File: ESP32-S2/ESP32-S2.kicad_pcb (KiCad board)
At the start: 2 copper layers, 27.9 x 70 mm, 39 parts, among them J1 Conn_01x18_Male, J2 Conn_01x21_Male, J3 USB_A, J4 TYPE-C-31-M-12, Q2 L8050QLT1G, Q3 L8050QLT1G, SW1 EN/RESET, SW2 BOOT/SELECT, U2 ESP32-S2-WROOM-ESP32-S2-WROOM, U3 AMS1117-3.3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

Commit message: Routing Updates
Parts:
- moved SW2 0.39 mm to (159.2, 119.5)
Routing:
- net GND: track 174.1 -> 108.1 mm, vias 8 -> 5
- net /GPIO0: track 82.5 -> 107.3 mm, vias 10 -> 6
- net /CHIP_PU: track 78.7 -> 83.2 mm
- net /GPIO19: track 50.1 -> 52.8 mm
- net /GPIO11: track 21.0 -> 18.4 mm
- net /GPIO12: track 22.4 -> 20.1 mm
- net /GPIO10: track 18.9 -> 16.9 mm
- net /TXD0: track 46.6 -> 44.8 mm
- net /DN1: track 43.2 -> 41.5 mm
- net /GPIO9: track 16.8 -> 15.3 mm
- net /GPIO15: track 22.6 -> 21.3 mm, vias 2 -> 0
- net /GPIO26: track 18.9 -> 18.4 mm
- net /GPIO17: track 33.9 -> 34.3 mm, vias 2 -> 0
- net /GPIO20: track 76.3 -> 76.6 mm, vias 4 -> 2

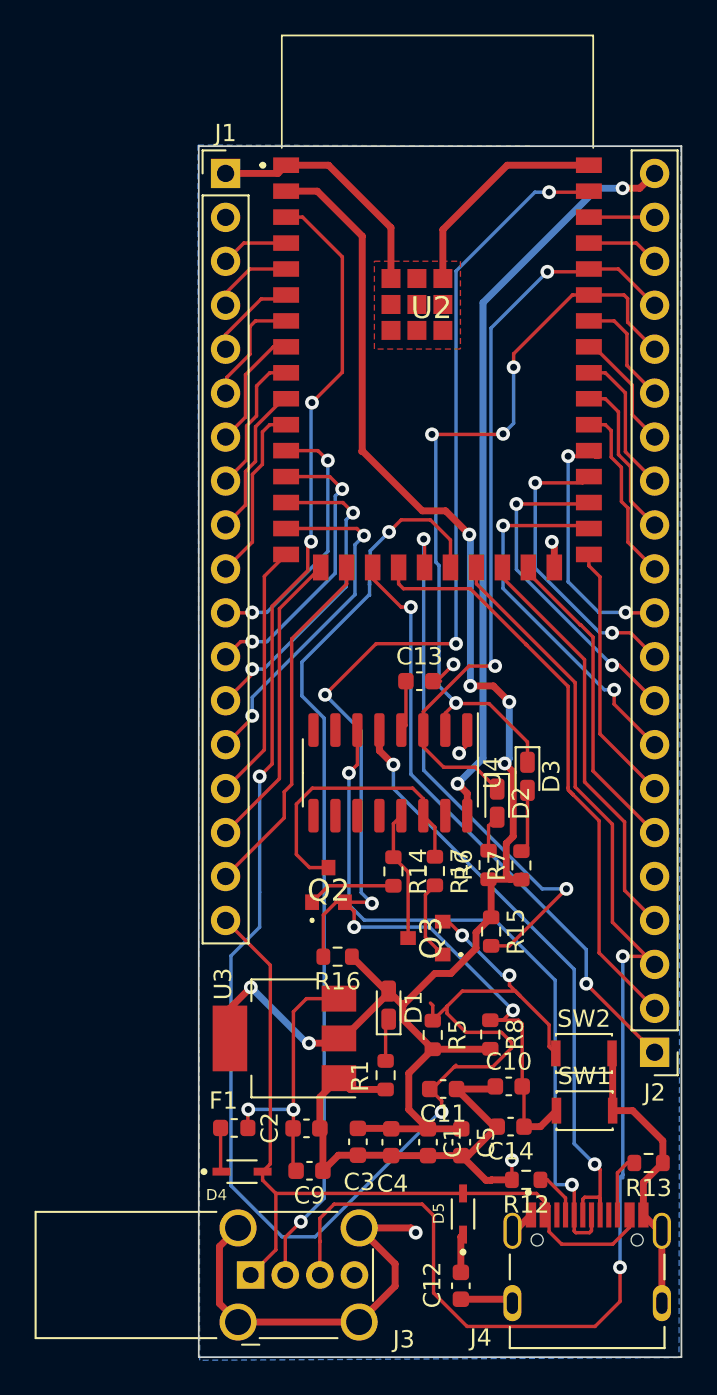
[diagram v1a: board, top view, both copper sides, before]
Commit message: Cleaned up routing
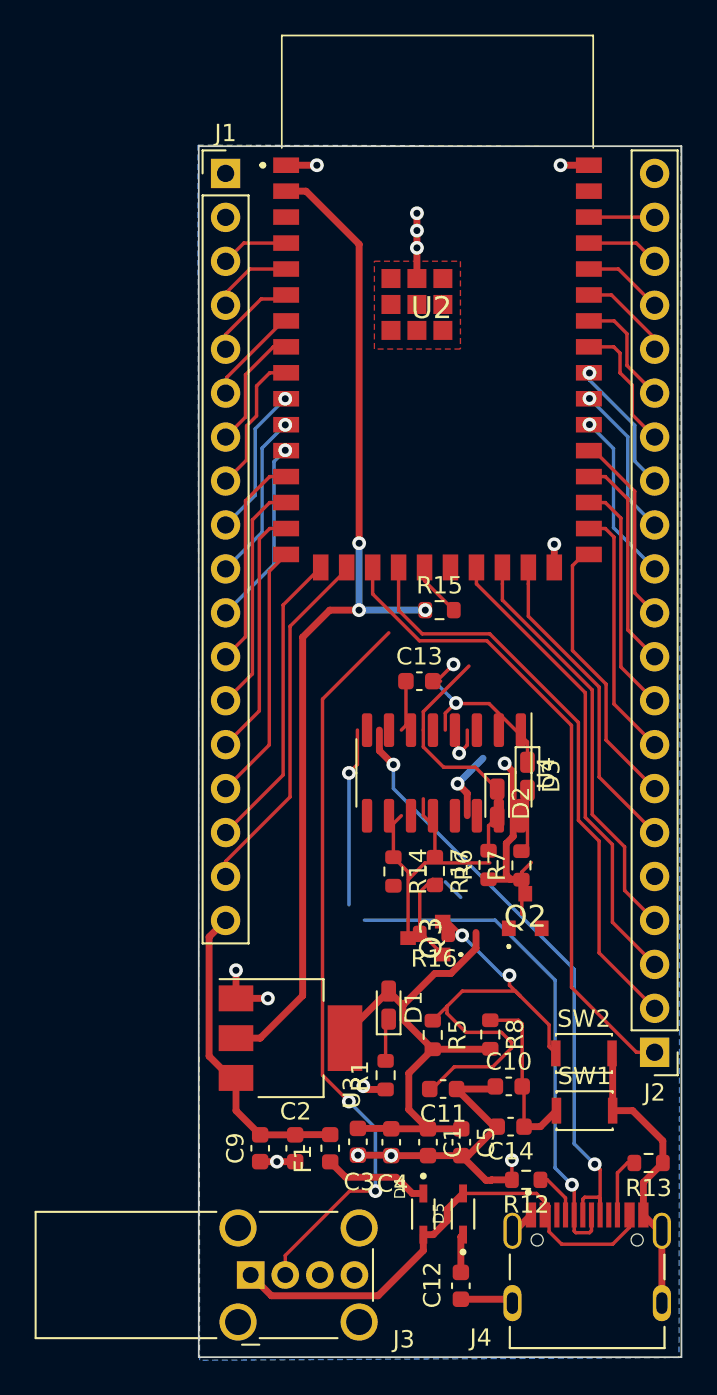
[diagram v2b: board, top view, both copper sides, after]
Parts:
- moved R15 18.8 mm to (150.8, 93.9), turned to 0 degrees
- moved Q2 11.5 mm to (155.8, 111.3)
- moved D4 10.8 mm to (149.9, 128.8), turned to 270 degrees
- moved R16 5.73 mm to (150.5, 112.6)
- moved F1 5.67 mm to (144.5, 125.0), turned to 270 degrees
- moved C9 3.13 mm to (140.4, 125.0), turned to 90 degrees
- moved U4 3.10 mm to (151.1, 103.3)
- moved C2 1.32 mm to (142.5, 125.0), turned to 270 degrees
- moved U3 0.35 mm to (142.2, 118.7), turned to 0 degrees
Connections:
- J1 pad 18: /VBUS -> /VI
- SW1 pad 1: /CHIP_PU -> GND
- SW2 pad 1: /GPIO0 -> GND
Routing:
- net /GPIO0: track 107.3 -> 27.5 mm, vias 6 -> 2
- net /CHIP_PU: track 83.2 -> 14.2 mm, vias 6 -> 0
- net /GPIO20: track 76.6 -> 27.9 mm, vias 2 -> 0
- net GND: track 108.1 -> 61.1 mm, vias 5 -> 15
- net VCC: track 43.5 -> 4.16 mm, vias 2 -> 1
- net /TXD0: track 44.8 -> 14.9 mm, vias 4 -> 1
- net /GPIO18: track 31.8 -> 3.17 mm, vias 2 -> 0
- net /RXD0: track 43.9 -> 15.9 mm, vias 2 -> 0
- net /VBUS: track 47.5 -> 30.1 mm
- net /~RTS: track 16.7 -> 3.63 mm
- net /GPIO19: track 52.8 -> 43.0 mm
- net /GPIO34: track 21.7 -> 14.9 mm, vias 2 -> 0
- net +3V3: track 96.9 -> 102.9 mm, vias 6 -> 4
- net /GPIO12: track 20.1 -> 14.5 mm, vias 2 -> 0
- net /GPIO35: track 19.1 -> 13.6 mm, vias 2 -> 0
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
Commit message: Updated Routing
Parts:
- moved R16 2.80 mm to (147.9, 113.8)
- moved C13 1.32 mm to (150.9, 97.7)
- moved Q3 0.86 mm to (149.5, 112.2)
- moved Q2 0.74 mm to (155.8, 112.0)
- moved D3 0.64 mm to (156.5, 103.5)
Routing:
- net /CHIP_PU: track 14.2 -> 77.7 mm, vias 0 -> 4
- net /GPIO0: track 27.5 -> 86.5 mm, vias 2 -> 4
- net VCC: track 4.16 -> 44.6 mm, vias 1 -> 3
- net /GPIO20: track 27.9 -> 63.0 mm, vias 0 -> 1
- net GND: track 61.1 -> 92.7 mm, vias 15 -> 16
- net /TXD0: track 14.9 -> 38.5 mm, vias 1 -> 3
- net /RXD0: track 15.9 -> 38.8 mm, vias 0 -> 3
- net /GPIO19: track 43.0 -> 61.3 mm, vias 2 -> 4
- net /~RTS: track 3.63 -> 10.1 mm, vias 0 -> 2
- net Net-(Q3-Pad1): track 1.41 -> 4.91 mm
- net Net-(Q2-Pad1): track 5.09 -> 8.55 mm, vias 0 -> 2
- net /DP1: track 36.2 -> 39.1 mm
- net /~DTR: track 7.62 -> 10.5 mm
- net +3V3: track 102.9 -> 101.6 mm, vias 4 -> 3
- net Net-(D3-Pad2): track 3.66 -> 4.61 mm
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
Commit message: Updated Routing
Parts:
- moved D2 9.48 mm to (144.8, 103.4)
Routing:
- net /DN1: track 38.9 -> 55.1 mm
- net Net-(D2-Pad2): track 2.14 -> 12.8 mm
- net /RXD0: track 38.8 -> 48.1 mm, vias 3 -> 5
- net GND: track 92.7 -> 84.0 mm
- net +3V3: track 101.6 -> 109.1 mm
- net /GPIO20: track 63.0 -> 69.9 mm, vias 1 -> 3
- net /TXD0: track 38.5 -> 43.4 mm
- net /CHIP_PU: track 77.7 -> 81.0 mm
- net /DP1: track 39.1 -> 37.3 mm, vias 2 -> 4
- net /GPIO33: track 16.1 -> 15.1 mm
- net VCC: track 44.6 -> 43.8 mm
- net /GPIO19: track 61.3 -> 60.6 mm
- net /GPIO16: track 37.7 -> 38.4 mm
- net /GPIO17: track 33.9 -> 34.6 mm
- net Net-(Q2-Pad1): track 8.55 -> 9.17 mm, vias 2 -> 0
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
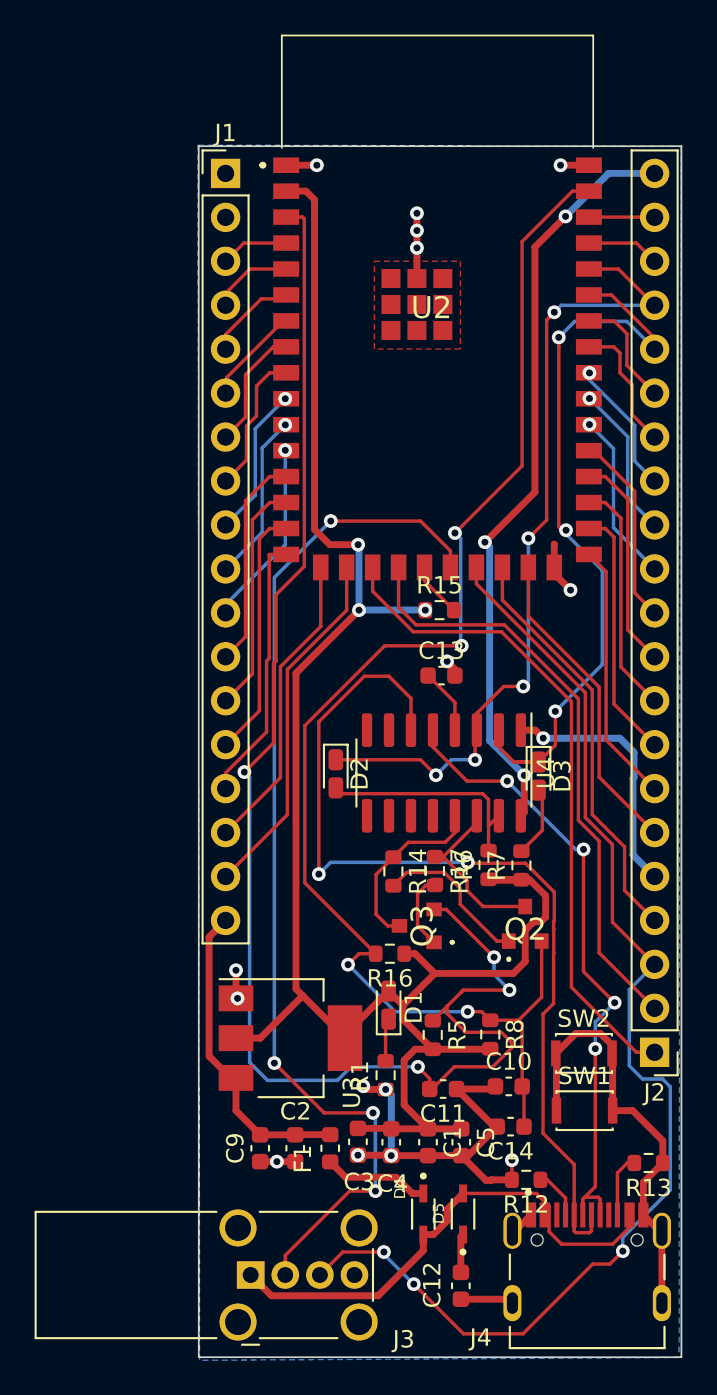
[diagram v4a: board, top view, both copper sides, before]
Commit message: optimised routing further
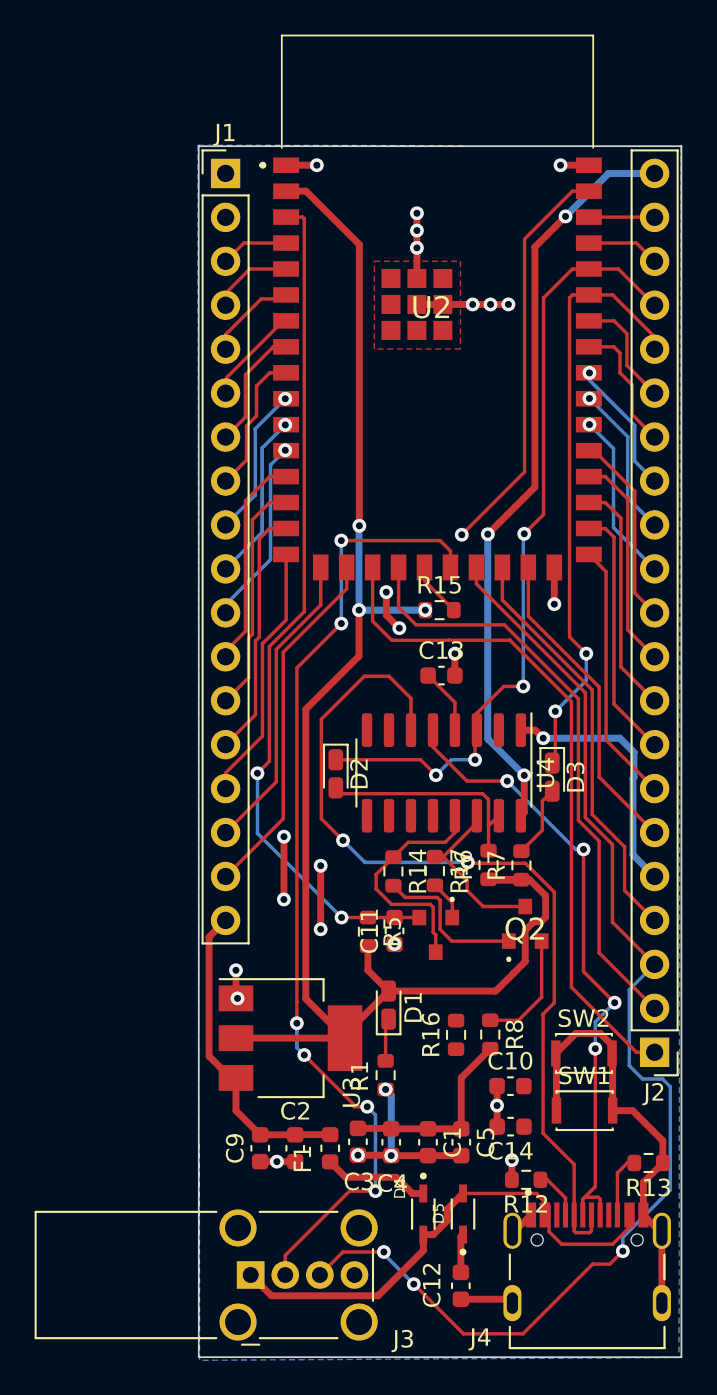
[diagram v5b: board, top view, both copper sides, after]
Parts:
- moved C11 9.56 mm to (148.2, 112.5), turned to 90 degrees
- moved R5 7.04 mm to (146.7, 112.5)
- moved R16 6.05 mm to (151.8, 118.5), turned to 90 degrees
- moved Q3 1.21 mm to (150.6, 112.7), turned to 180 degrees
- moved D3 0.80 mm to (157.3, 103.6)
- moved C10 0.10 mm to (154.9, 121.4)
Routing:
- net /CHIP_PU: track 81.0 -> 30.8 mm, vias 4 -> 1
- net /GPIO0: track 86.5 -> 49.1 mm, vias 4 -> 2
- net /TXD0: track 43.4 -> 34.8 mm, vias 3 -> 2
- net +3V3: track 109.1 -> 101.6 mm
- net /GPIO19: track 60.6 -> 56.4 mm, vias 4 -> 6
- net GND: track 84.0 -> 87.6 mm, vias 16 -> 26
- net /~DTR: track 10.5 -> 13.8 mm
- net /DN1: track 55.1 -> 52.5 mm
- net Net-(Q3-Pad1): track 4.91 -> 2.27 mm
- net /RXD0: track 48.1 -> 46.0 mm, vias 5 -> 4
- net /GPIO16: track 38.4 -> 39.4 mm
- net /GPIO13: track 15.5 -> 15.0 mm

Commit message: Updated Routing
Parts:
- moved C14 27.1 mm to (149.0, 97.4), turned to 270 degrees
- moved C10 25.2 mm to (147.3, 97.4), turned to 90 degrees
- moved R16 21.1 mm to (150.6, 97.4)
- moved R8 21.1 mm to (152.2, 97.4)
- moved SW1 7.59 mm to (151.9, 120.7)
- moved SW2 7.44 mm to (151.9, 117.8)
- moved R13 7.18 mm to (155.8, 124.7), turned to 90 degrees
- moved C12 3.91 mm to (152.9, 129.2), turned to 90 degrees
- moved C13 2.95 mm to (153.9, 97.4), turned to 90 degrees
- moved R12 2.81 mm to (154.0, 124.7), turned to 90 degrees
- moved D5 1.12 mm to (151.1, 129.0)
- moved D4 0.97 mm to (148.9, 128.9)
- moved C2 0.40 mm to (142.5, 124.6)
- moved C9 0.40 mm to (140.4, 124.6)
- moved F1 0.40 mm to (144.5, 124.6)
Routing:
- net /CHIP_PU: track 30.8 -> 58.2 mm, vias 1 -> 4
- net GND: track 87.6 -> 67.3 mm, vias 26 -> 24
- net +3V3: track 101.6 -> 115.9 mm, vias 3 -> 14
- net /VBUS: track 30.1 -> 36.8 mm, vias 0 -> 5
- net /GPIO20: track 69.9 -> 63.3 mm
- net /TXD0: track 34.8 -> 39.4 mm
- net /CC2: track 3.64 -> 7.16 mm, vias 0 -> 2
- net /CC1: track 2.86 -> 6.00 mm
- net /DN1: track 52.5 -> 51.1 mm
- net Net-(D4-PadC): track 6.14 -> 5.22 mm
- net /RXD0: track 46.0 -> 45.4 mm
- net /GPIO33: track 15.1 -> 15.7 mm
- net /GPIO16: track 39.4 -> 39.9 mm
- net /GPIO19: track 56.4 -> 56.7 mm, vias 6 -> 4

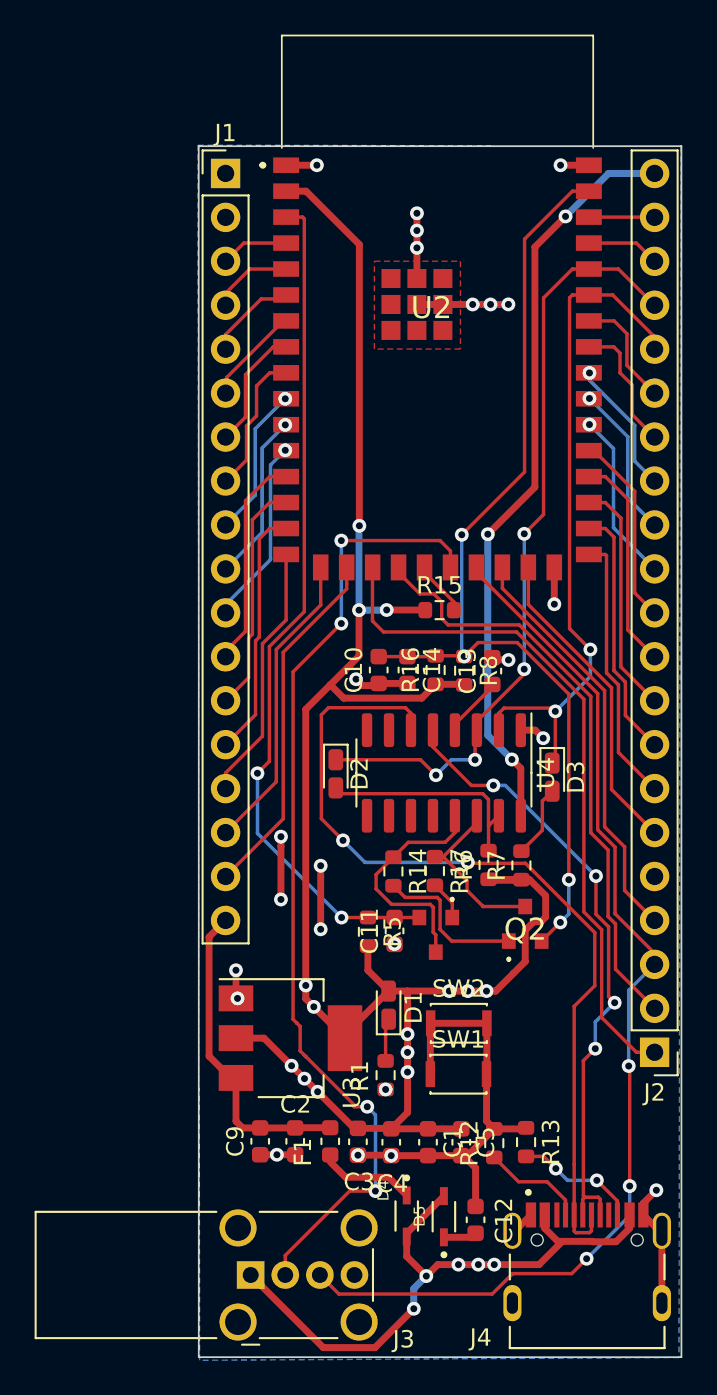
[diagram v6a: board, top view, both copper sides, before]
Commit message: Switches added
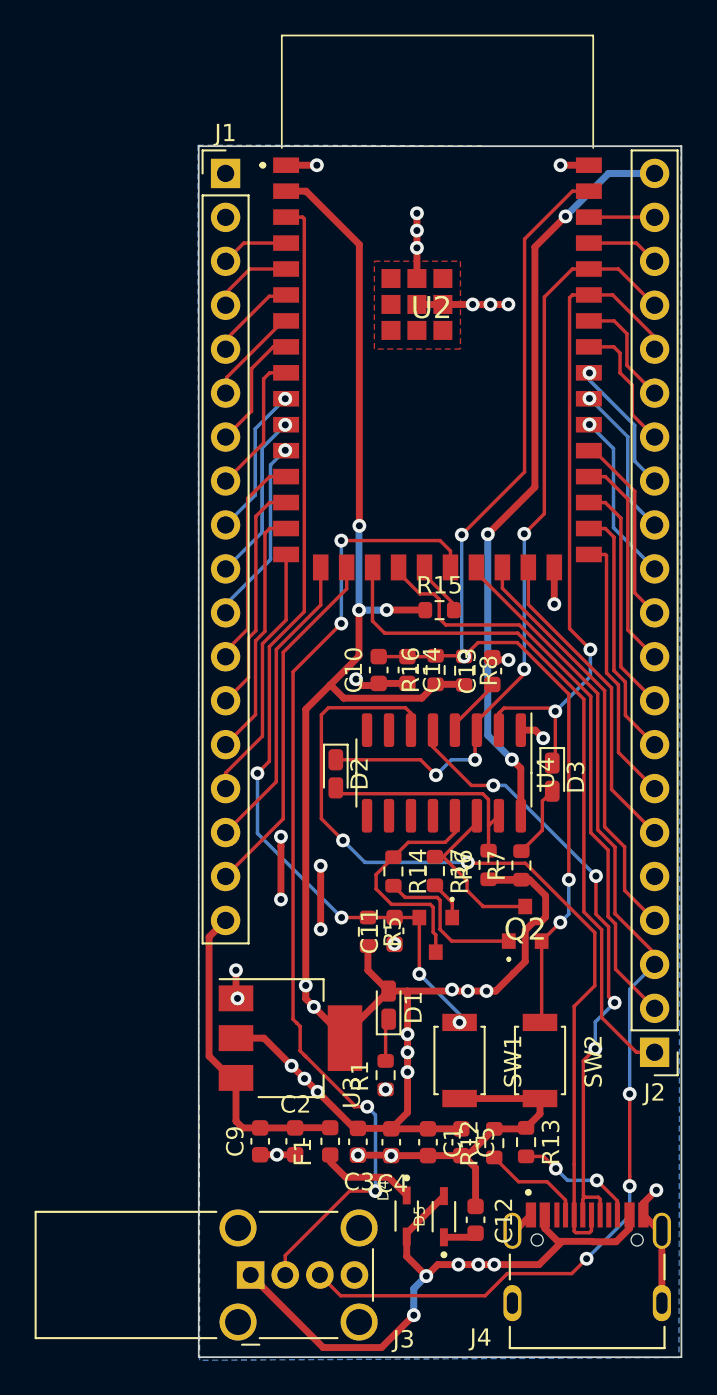
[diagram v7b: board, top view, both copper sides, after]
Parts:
- SW1: value EN/RESET -> SW_Push; footprint Button_Switch_SMD:SW_SPST_CK_KXT3 -> tactile_smd_switch:tactile_smd_switch
- SW2: value BOOT/SELECT -> SW_Push; footprint Button_Switch_SMD:SW_SPST_CK_KXT3 -> tactile_smd_switch:tactile_smd_switch
- moved SW2 5.16 mm to (156.6, 120.0), turned to 90 degrees
- moved SW1 0.79 mm to (152.0, 120.0), turned to 90 degrees
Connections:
- SW1 pad 2: GND -> /GPIO0
- SW2 pad 2: GND -> /CHIP_PU
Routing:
- net /GPIO0: track 49.1 -> 56.1 mm, vias 2 -> 4
- net GND: track 67.3 -> 61.4 mm
- net /CHIP_PU: track 58.2 -> 62.9 mm

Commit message: added 3D models
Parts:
- moved J2 50.8 mm to (163.2, 68.7), turned to 0 degrees
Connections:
- J2 pad 1: /GPIO16 -> VCC
- J2 pad 10: /GPIO36 -> /GPIO38
- J2 pad 12: /GPIO38 -> /GPIO36
- J2 pad 13: /GPIO39 -> /GPIO35
- J2 pad 14: /SCL -> /GPIO34
- J2 pad 15: /SDA -> /GPIO33
- J2 pad 16: /GPIO42 -> /GPIO26
- J2 pad 17: /TXD0 -> GND
- J2 pad 18: /RXD0 -> /GPIO21
- J2 pad 19: /GPIO45 -> /GPIO20
- J2 pad 2: /GPIO17 -> /GPIO46
- J2 pad 20: /GPIO46 -> /GPIO17
- J2 pad 21: VCC -> /GPIO16
- J2 pad 3: /GPIO20 -> /GPIO45
- J2 pad 4: /GPIO21 -> /RXD0
- J2 pad 5: GND -> /TXD0
- J2 pad 6: /GPIO26 -> /GPIO42
- J2 pad 7: /GPIO33 -> /SDA
- J2 pad 8: /GPIO34 -> /SCL
- J2 pad 9: /GPIO35 -> /GPIO39
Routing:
- net +3V3: track 116.0 -> 124.5 mm, vias 14 -> 16
- net /DN1: track 51.1 -> 50.2 mm
- net Net-(D2-Pad2): track 12.8 -> 12.1 mm
- net /GPIO20: track 63.3 -> 62.7 mm
- net /GPIO33: track 15.7 -> 15.1 mm
